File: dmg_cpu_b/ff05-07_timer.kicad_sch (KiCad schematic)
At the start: 75 parts

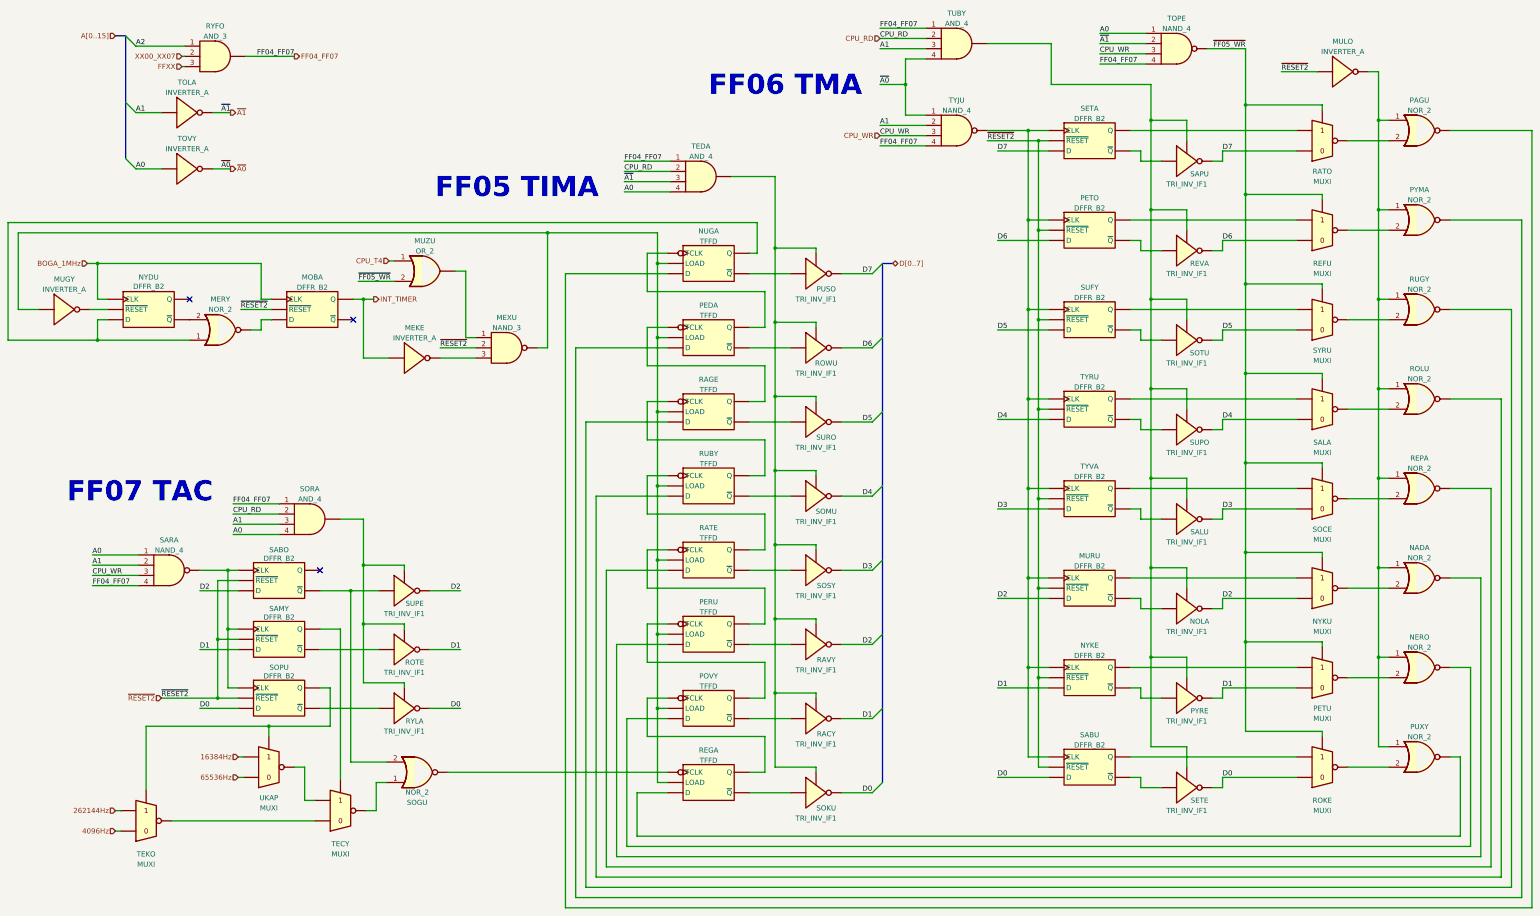
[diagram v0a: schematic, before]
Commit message: Give more meaningful names to cell types
Before this commit, many of the cells types in the chip were named in a
sloppy manner. The different inverter, latch and flip flop valiants were
just suffixed with A, B, C, D, ... Those suffixes gave no information
about the actual differences. They had to be looked up in the
documentation. Now the names of cell types with different variants have
changed:

* Inverter types are named NOT_X1, NOT_X2, NOT_X3, ... The _Xn suffix
  reflects the drive strength of the cell. X1 is the drive strength of
  the weakest inverter, X2 is double the drive strength of the weakest
  inverter.
* Flip flop types are named DFFR, DFFR_CC, DFFR_CC_Q. DFFR is a normal
  data flip flop with reset and a single clock input. The suffix _CC is
  added to flip flops that have two complementary clock inputs (CLK and
  /CLK). Flip flops that only have the positive Q output are suffixed
  with _Q.
* Latch types are named similar to flip flops: DLATCH, DLATCH_EE,
  DLATCH_EE_Q. The suffix _EE is given to latches that require
  "externally inverted enable" signals (ENA and /ENA).
* I/O pad types all start with PAD_BIDIR, PAD_IN or PAD_OUT. They also
  have suffixes that describe what makes them unique, like _PU for
  pull-ups.

Other minor changes were made to align the names with common naming
schemes of other cell libraries.
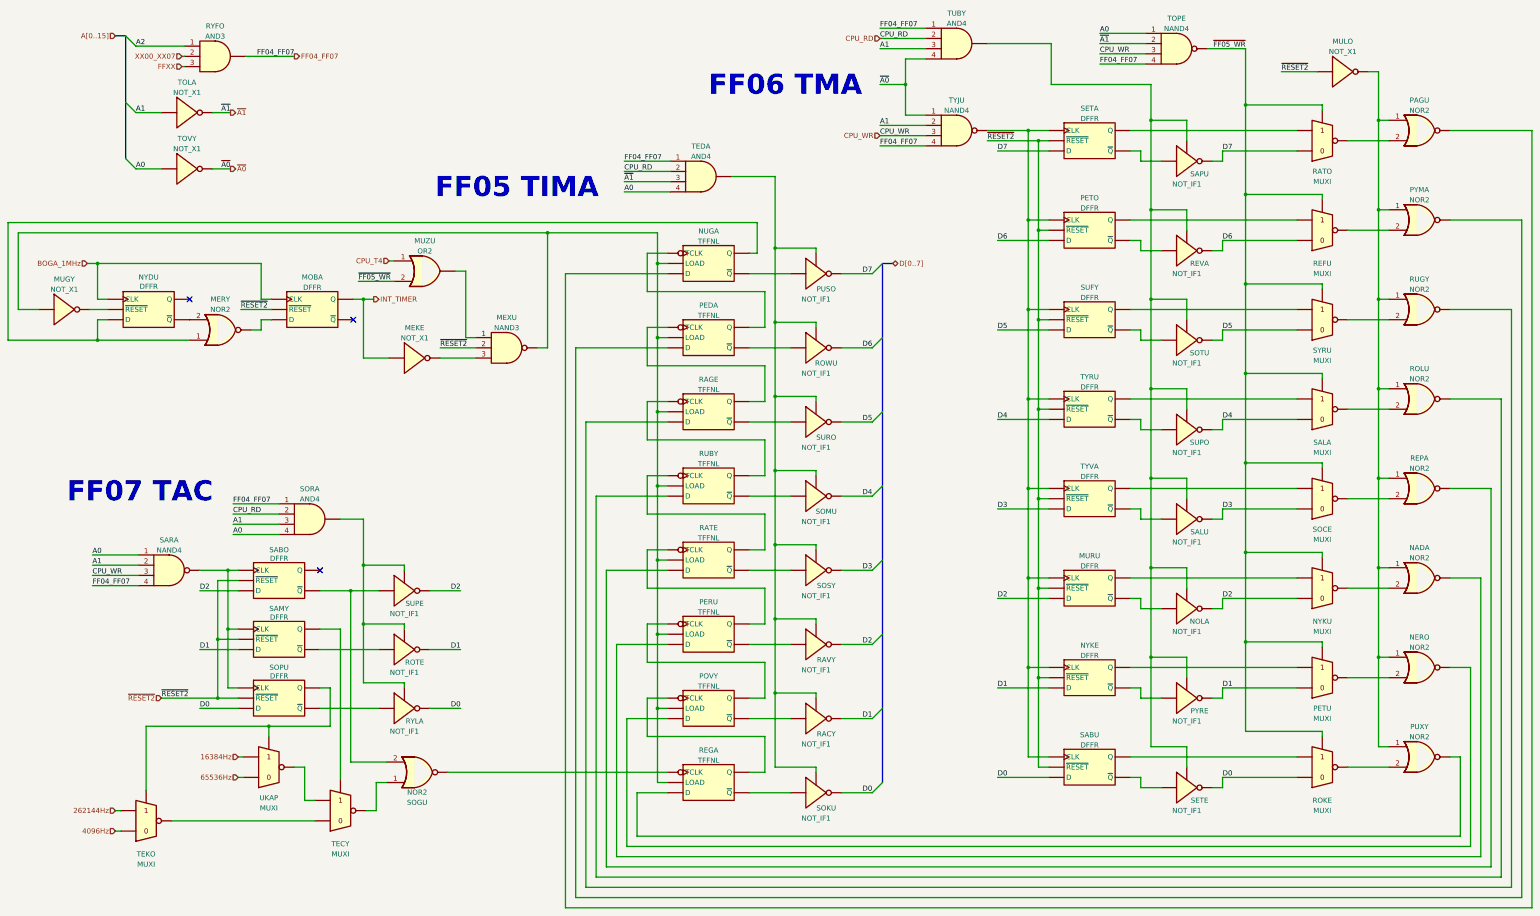
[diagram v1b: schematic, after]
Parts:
- MEKE, MUGY, MULO, TOLA, TOVY: value INVERTER_A -> NOT_X1; symbol DMG_CPU_Cells:INVERTER_A -> DMG_CPU_Cells:NOT_X1
- MERY, NADA, NERO, PAGU, PUXY, PYMA, REPA, ROLU, RUGY, SOGU: value NOR_2 -> NOR2; symbol DMG_CPU_Cells:NOR_2 -> DMG_CPU_Cells:NOR2
- MEXU: value NAND_3 -> NAND3; symbol DMG_CPU_Cells:NAND_3 -> DMG_CPU_Cells:NAND3
- MOBA, MURU, NYDU, NYKE, PETO, SABO, SABU, SAMY, SETA, SOPU, SUFY, TYRU, TYVA: value DFFR_B2 -> DFFR; symbol DMG_CPU_Cells:DFFR_B2 -> DMG_CPU_Cells:DFFR
- MUZU: value OR_2 -> OR2; symbol DMG_CPU_Cells:OR_2 -> DMG_CPU_Cells:OR2
- NOLA, PUSO, PYRE, RACY, RAVY, REVA, ROTE, ROWU, RYLA, SALU, SAPU, SETE, SOKU, SOMU, SOSY, SOTU, SUPE, SUPO, SURO: value TRI_INV_IF1 -> NOT_IF1; symbol DMG_CPU_Cells:TRI_INV_IF1 -> DMG_CPU_Cells:NOT_IF1
- NUGA, PEDA, PERU, POVY, RAGE, RATE, REGA, RUBY: value TFFD -> TFFNL; symbol DMG_CPU_Cells:TFFD -> DMG_CPU_Cells:TFFNL
- RYFO: value AND_3 -> AND3; symbol DMG_CPU_Cells:AND_3 -> DMG_CPU_Cells:AND3
- SARA, TOPE, TYJU: value NAND_4 -> NAND4; symbol DMG_CPU_Cells:NAND_4 -> DMG_CPU_Cells:NAND4
- SORA, TEDA, TUBY: value AND_4 -> AND4; symbol DMG_CPU_Cells:AND_4 -> DMG_CPU_Cells:AND4

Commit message: SM83 Layout: Add bottom part of sequencer cells
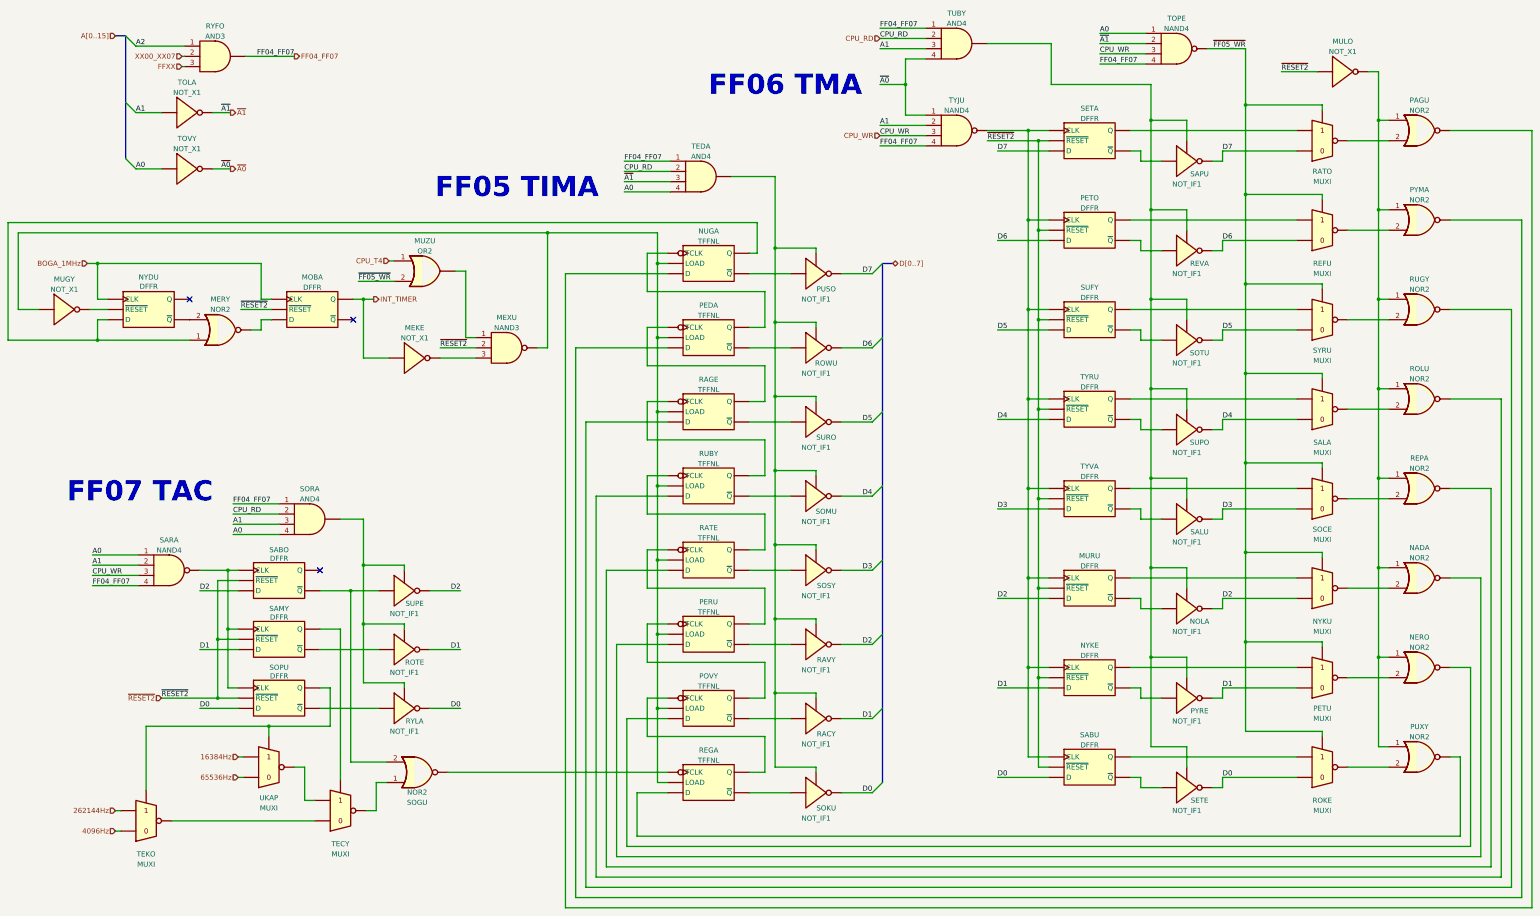
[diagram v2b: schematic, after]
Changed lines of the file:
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@@
 (kicad_sch
-	(version 20231120)
+	(version 20250114)
 	(generator "eeschema")
-	(generator_version "8.0")
+	(generator_version "9.0")
 	(paper "A3")
 	(title_block
 		(title "DMG-CPU B")
-		(date "2025-04-12")
+		(date "2025-04-22")
 		(rev "0.7")
 		(company "CC-BY-SA-4.0 Régis Galland & Michael Singer -- Derived work from Furrtek")
 		(comment 1 "https://github.com/msinger/dmg-schematics")
 	)
+	(text "FF07 TAC\n"
+		(exclude_from_sim no)
+		(at 31.75 142.24 0)
+		(effects
+			(font
+				(size 5 5)
+				(thickness 1)
+				(bold yes)
+			)
+			(justify left bottom)
+		)
+	)
+	(text "FF05 TIMA"
+		(exclude_from_sim no)
+		(at 123.19 66.675 0)
+		(effects
+			(font
+				(size 5 5)
+				(thickness 1)
+				(bold yes)
+			)
+			(justify left bottom)
+		)
+	)
+	(text "FF06 TMA"
+		(exclude_from_sim no)
+		(at 191.135 41.275 0)
+		(effects
+			(font
+				(size 5 5)
+				(thickness 1)
+				(bold yes)
+			)
+			(justify left bottom)
+		)
+	)
 	(junction
 		(at 207.645 170.815)
@@
 		)
 	)
-	(text "FF07 TAC\n"
-		(exclude_from_sim no)
-		(at 31.75 142.24 0)
-		(effects
-			(font
-				(size 5 5)
-				(thickness 1)
-				(bold yes)
-			)
-			(justify left bottom)
-		)
-	)
-	(text "FF05 TIMA"
-		(exclude_from_sim no)
-		(at 123.19 66.675 0)
-		(effects
-			(font
-				(size 5 5)
-				(thickness 1)
-				(bold yes)
-			)
-			(justify left bottom)
-		)
-	)
-	(text "FF06 TMA"
-		(exclude_from_sim no)
-		(at 191.135 41.275 0)
-		(effects
-			(font
-				(size 5 5)
-				(thickness 1)
-				(bold yes)
-			)
-			(justify left bottom)
-		)
-	)

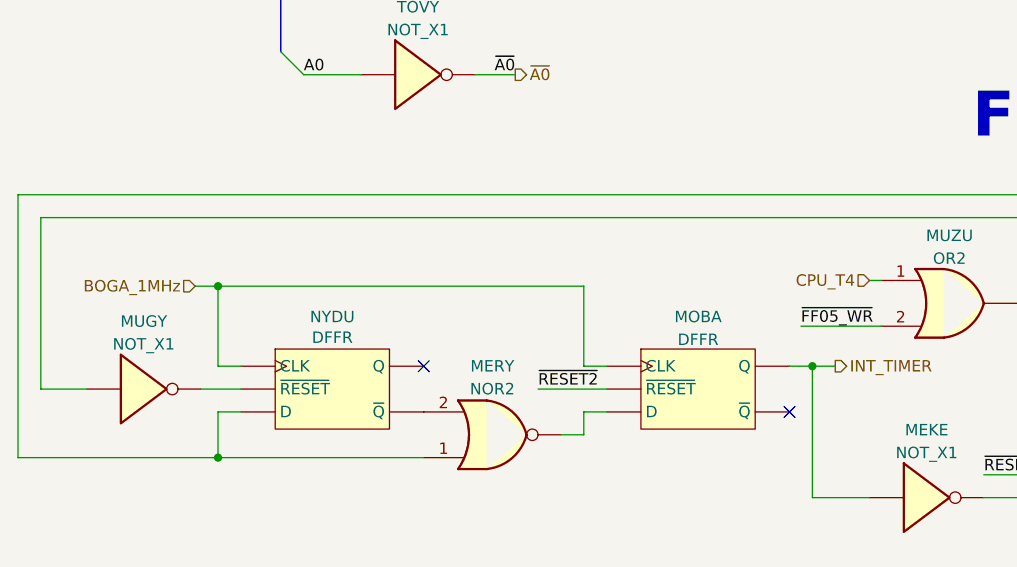
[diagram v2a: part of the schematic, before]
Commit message: DMG: Update CPU symbol and port names in schematic
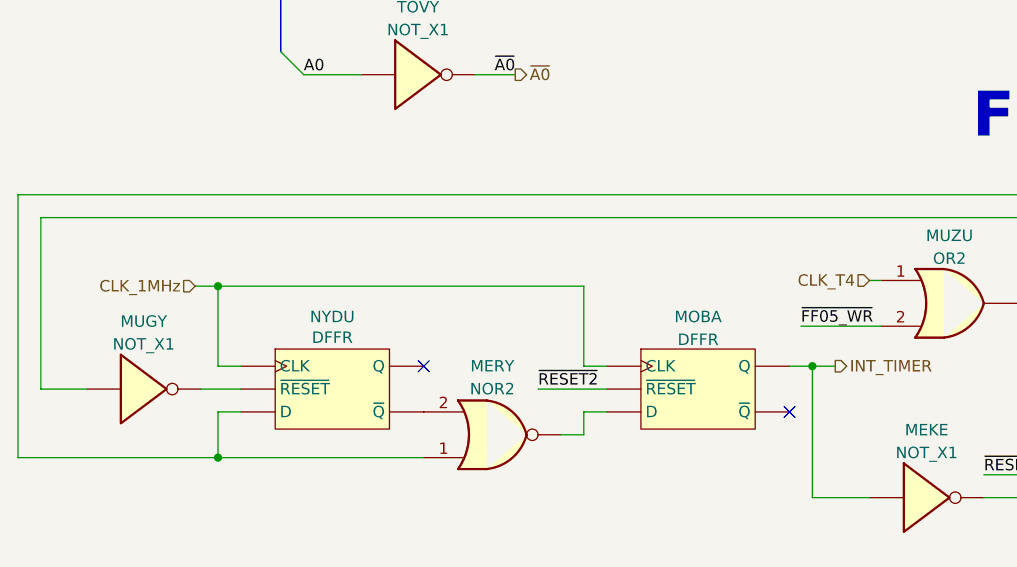
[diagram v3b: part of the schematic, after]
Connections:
- net BOGA_1MHz renamed CLK_1MHz
- net CPU_T4 renamed CLK_T4
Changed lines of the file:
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@@
 	(title_block
 		(title "DMG-CPU B")
-		(date "2025-04-22")
-		(rev "0.7")
+		(date "2025-11-28")
+		(rev "0.8")
 		(company "CC-BY-SA-4.0 Régis Galland & Michael Singer -- Derived work from Furrtek")
 		(comment 1 "https://github.com/msinger/dmg-schematics")
@@
 		)
 	)
-	(hierarchical_label "BOGA_1MHz"
+	(hierarchical_label "CLK_1MHz"
 		(shape input)
 		(at 36.83 82.55 180)
@@
 		)
 	)
-	(hierarchical_label "CPU_T4"
+	(hierarchical_label "CLK_T4"
 		(shape input)
 		(at 111.76 81.915 180)
